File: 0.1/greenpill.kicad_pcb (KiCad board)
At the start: 4 copper layers, 17.4 x 53.1 mm, 31 parts, among them J1 Conn_01x20_Male, J2 Conn_01x20_Male, J3 Conn_01x04_Male, J5 USB_C_Receptacle_USB2.0, SW1 SW_Push, SW2 SW_Push, U1 ATSAMD51J18A-M, U2 MIC5504-3.3YM5, U3 S25FL064, Y1 Crystal_GND23

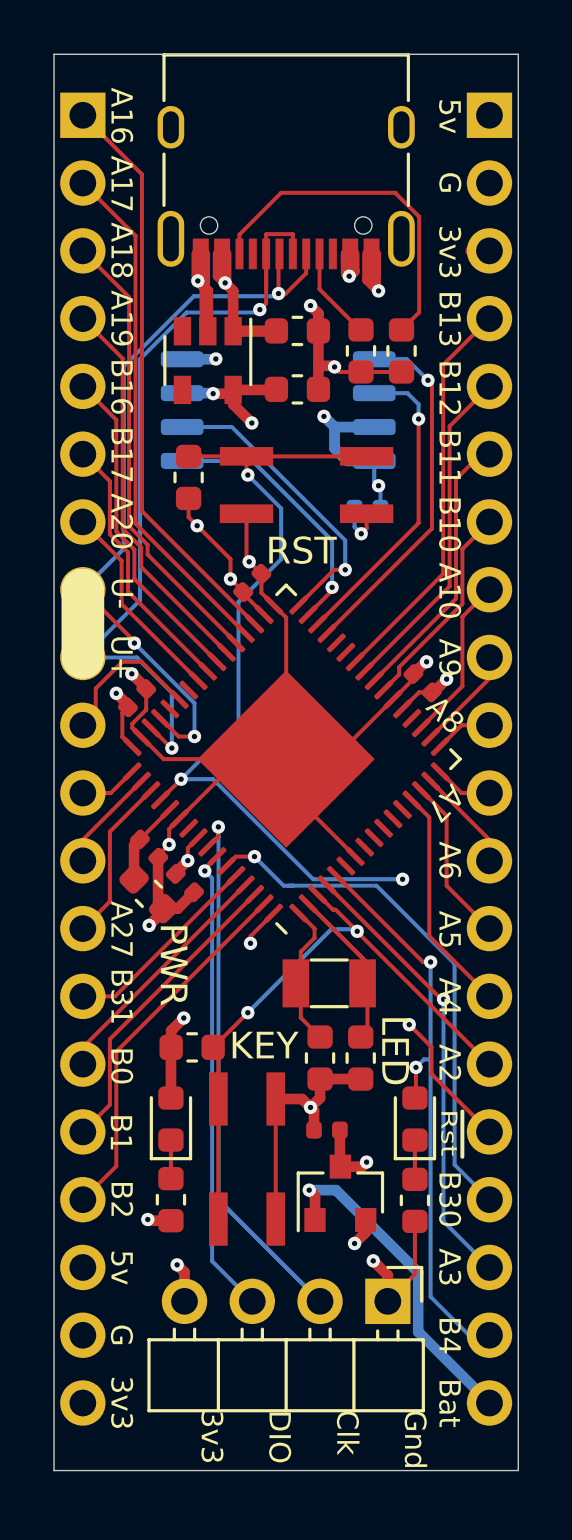
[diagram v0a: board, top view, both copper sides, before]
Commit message: Added * f u n k y * back silkscreen, some front silkscreen tweaks
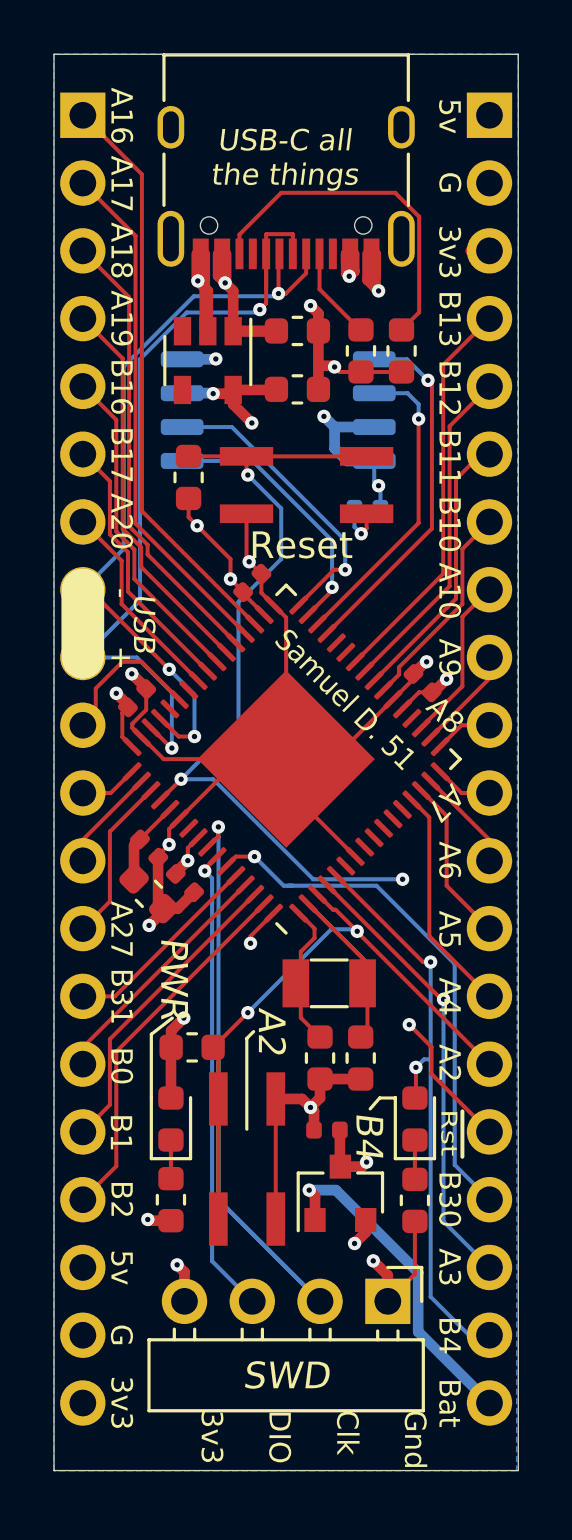
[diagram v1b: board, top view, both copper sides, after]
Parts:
- added REF**: OSHW-Symbol_4x4.5mm_SilkScreen, greenpill:OSHW-Symbol_4x4.5mm_SilkScreen, B.Cu at (135.6, 93.2)
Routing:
- added copper zone on B.Cu, net GND
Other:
- board text added: "+"
- board text added: "-"
- board text added: "@LukeMoll_"
- board text added: "@Stary2001"
- board text added: "Greenpill"
- board text added: "Reset"
- board text added: "SWD"
- board text added: "Samuel D. 51"
- board text added: "USB"
- board text added: "USB-C all the things"
- board text added: "github.com/Stary2001/Greenpill"
- board text removed: "1"
- board text removed: "10"
- board text removed: "11"
- board text removed: "12"
- board text removed: "13"
- board text removed: "14"
- board text removed: "15"
- board text removed: "16"
- board text removed: "17"
- board text removed: "18"
- board text removed: "19"
- board text removed: "2"
- board text removed: "20"
- board text removed: "21"
- board text removed: "22"
- board text removed: "23"
- board text removed: "24"
- board text removed: "25"
- board text removed: "26"
- board text removed: "27"
- board text removed: "28"
- board text removed: "29"
- board text removed: "3"
- board text removed: "30"
- board text removed: "31"
- board text removed: "32"
- board text removed: "4"
- board text removed: "5"
- board text removed: "6"
- board text removed: "7"
- board text removed: "8"
- board text removed: "9"
- board text removed: "KEY"
- board text removed: "LED"
- board text removed: "RST"
- board text removed: "U+"
- board text removed: "U-"

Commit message: swapped button and led to non broken out pins
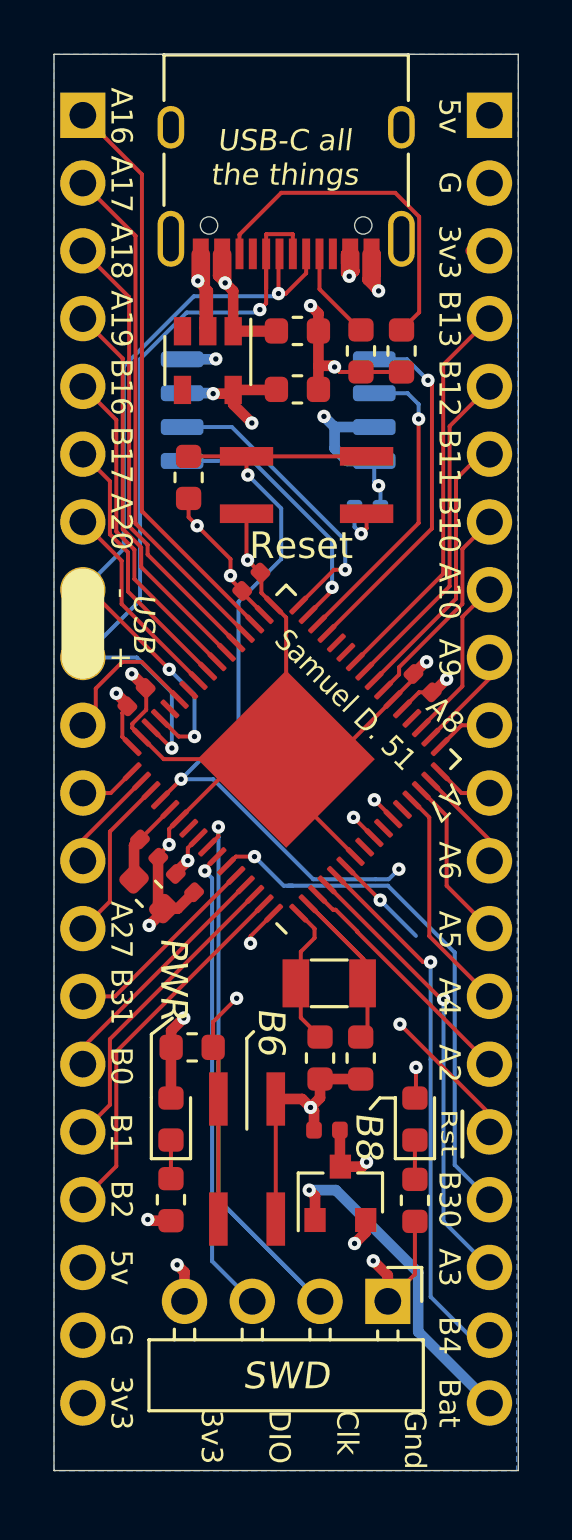
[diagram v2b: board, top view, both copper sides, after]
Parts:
- removed REF**: OSHW-Symbol_4x4.5mm_SilkScreen, greenpill:OSHW-Symbol_4x4.5mm_SilkScreen
- moved C1 0.06 mm to (134.3, 91.7)
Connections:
- D2 pad 2: /pb04 -> /pb08
- R6 pad 2: /pa02 -> /pb06
- SW2 pad 1: /pa02 -> /pb06
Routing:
- net /pb06: track 0.00 -> 19.1 mm, vias 0 -> 2
- net /pa02: track 22.9 -> 9.12 mm, vias 2 -> 0
- net /pb08: track 0.00 -> 13.0 mm, vias 0 -> 2
- net /pb05: track 0.00 -> 3.72 mm, vias 0 -> 1
- net /pb04: track 22.1 -> 20.2 mm, vias 2 -> 1
- net /!reset: track 42.9 -> 43.6 mm
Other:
- board text added: "B6"
- board text added: "B8"

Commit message: add mpns
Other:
- board text added: "not green"
- board text removed: "Greenpill"

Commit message: revert meme
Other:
- board text added: "Greenpill"
- board text removed: "not green"
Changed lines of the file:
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@@
     (effects (font (size 0.7 0.5) (thickness 0.08) italic) (justify left mirror))
   )
-  (gr_text "not green" (at 133.52 90.76 90) (layer B.SilkS)
+  (gr_text "Greenpill" (at 134.366 95.25 90) (layer B.SilkS)
     (effects (font (size 3 2.8) (thickness 0.6)) (justify left mirror))
   )
